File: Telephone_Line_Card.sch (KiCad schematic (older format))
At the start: 50 parts, among them J1 SULLINS EDGE 2X15 0.156\", J2 RJ11, K1 G5V-2, K2 TELTONE_M949-1, K3 G5V-2, Q6 2N3904, U1 4N35

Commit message: some schematic changes
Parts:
- removed C? (x2): 0.1uF, symbol Device:C
- removed C?: 0.047uF, symbol Device:C
- removed D?: 1N4148, Diode_THT:D_DO-35_SOD27_P7.62mm_Horizontal, symbol Diode:1N4148
- removed F?: Polyfuse, symbol Device:Polyfuse
- removed K1: G5V-2, Relay_THT:Relay_DPDT_Omron_G5V-2, symbol Relay:G5V-2
- removed Q?: 2N3904, Package_TO_SOT_THT:TO-92_Inline, symbol Transistor_BJT:2N3904
- removed R?: 10K, symbol Device:R_US
- removed R?: 1K, symbol Device:R_US
- removed TP1: GND, symbol Connector:TestPoint
- removed TP2: +12V, symbol Connector:TestPoint
- removed TP3: TESTPOINT(A), symbol Connector:TestPoint
- removed TP4: TESTPOINT(B), symbol Connector:TestPoint
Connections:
- net LINE1A is gone; now on net VOICE_LINE(T): J1.24 (Pin_24)
- net LINE1B is gone; now on net VOICE_LINE(R): J1.23 (Pin_23)
- net RING_TRIP: no longer J1.26 (Pin_26), R?.2, U1.5
- net VOICE_LINE(T): now reaches D?.1 (K), D?.2 (A)
- net VOICE_LINE(T): now also T?.8 (SB)
- net VOICE_LINE(R): now reaches D?.1 (K), D?.2 (A)
- net VOICE_LINE(R): now also T?.5 (SA)
- net LINE2A: no longer names the net of J1.22 (Pin_22)
- net LINE2B: no longer names the net of J1.21 (Pin_21)
- net LS: no longer names the net of J1.29 (Pin_29)
- net RING_BUS_R renamed RING_BUS(R)
- net RING_BUS_T renamed RING_BUS(T)
- new net RT: J1.26 (Pin_26), R?.2, U1.5
- no-connect marks 10 -> 13
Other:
- note added: "PROTOTYPE!"
- note removed: "*ADD RESISTORS INLINE?\n*ISOLATION TRANSFORMER \nBEFORE OR AFTER VOICE RELAY?"
- note removed: "PELIMINARY PROTOTYPE!"
- note removed: "VOICE LINE RELAY"
- moved on the sheet: D?

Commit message: some schematic changes
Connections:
- net RING_TRIP is gone; now on net RT: R?.1
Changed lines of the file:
@@
 Wire Wire Line
 	10320 3390 10610 3390
-Text Notes 11630 4290 0    50   ~ 0
+Text Notes 11640 4270 0    50   ~ 0
 RING TRIP CIRCUIT\nSEE "TRIX V2" FIG 19 FOR MORE DETAILS
 Text Notes 8390 8330 0    50   ~ 0
@@
 Wire Wire Line
 	10090 4960 10320 4960
-Text Notes 720  1500 0    500  ~ 0
+Text Notes 1410 1890 0    500  ~ 0
 PROTOTYPE!
 Connection ~ 11280 2740
@@
 	13390 7630 13390 8130
 Text GLabel 12570 8330 0    50   Input ~ 0
-RING_TRIP
+RT
 $Comp
 L Device:R_US R?

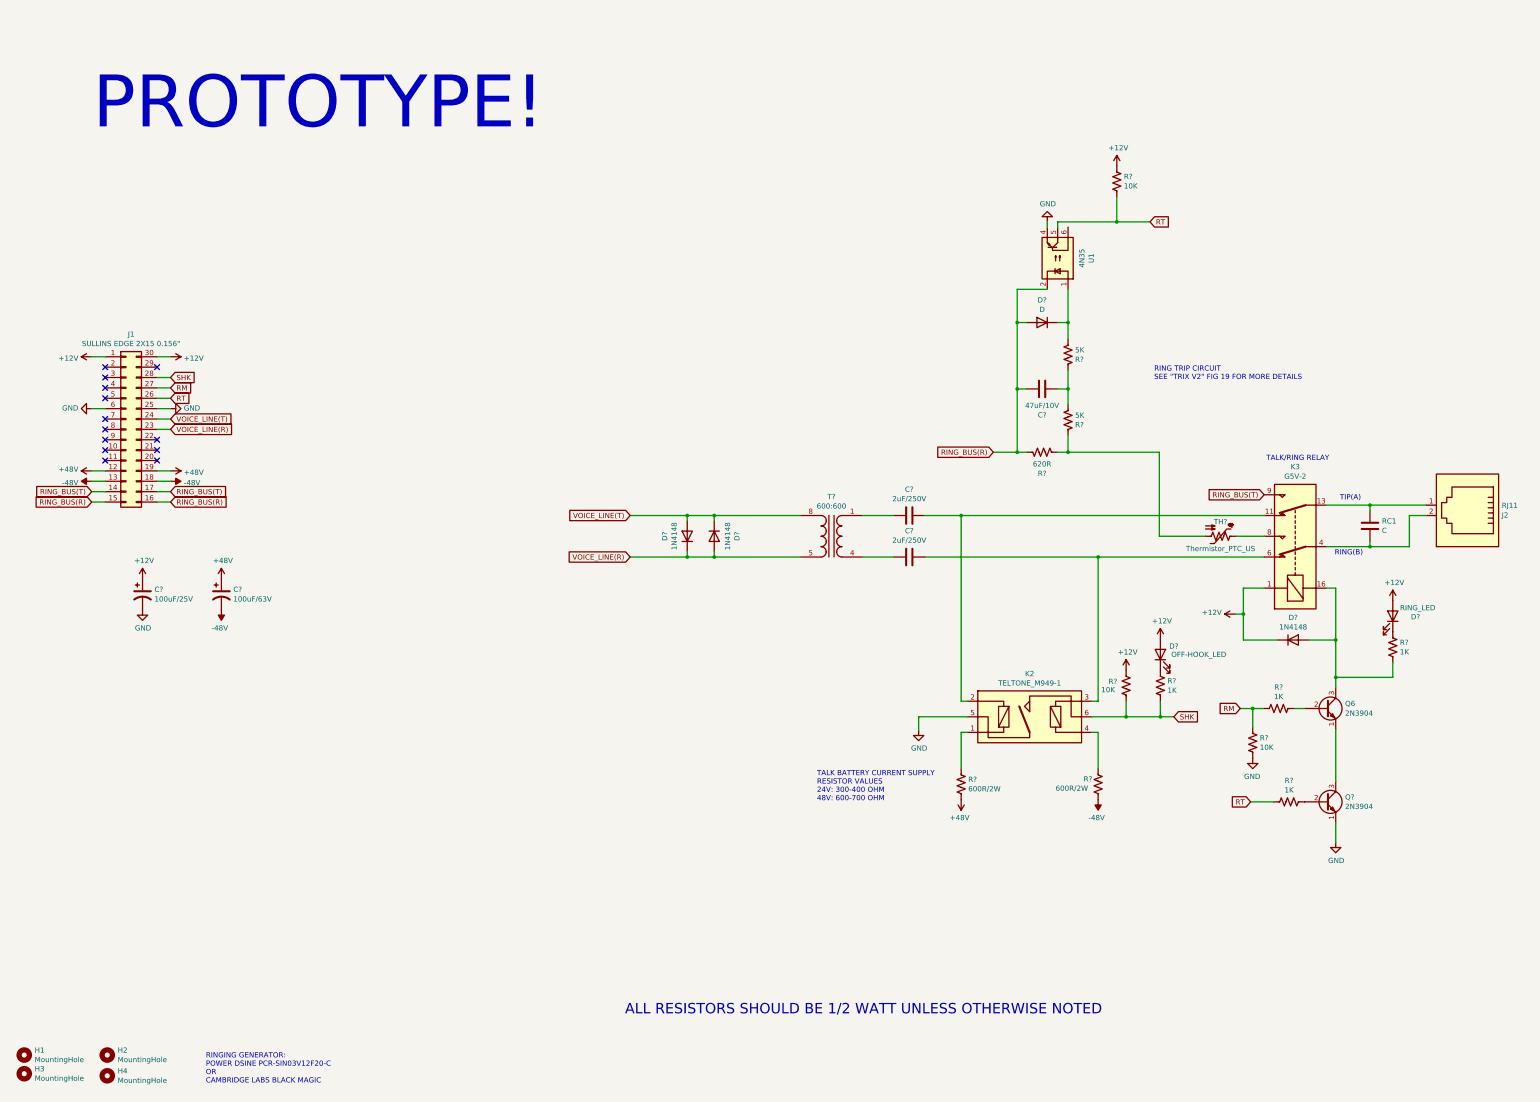
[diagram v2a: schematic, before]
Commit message: added slic sch symbol
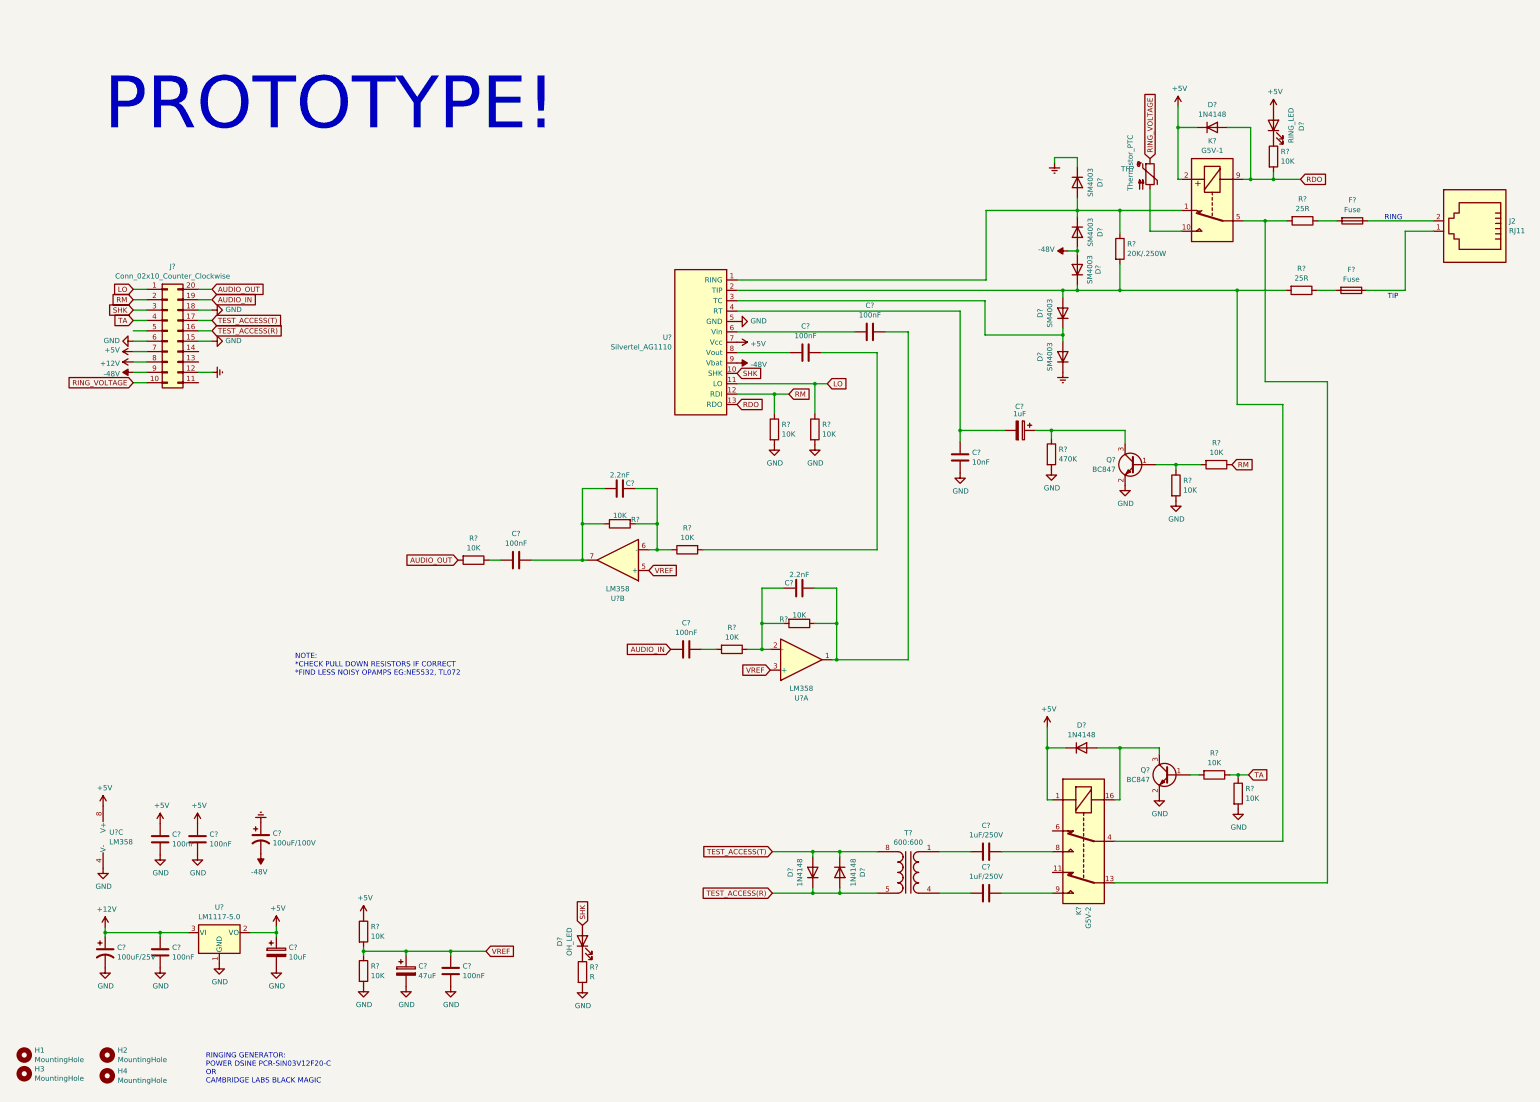
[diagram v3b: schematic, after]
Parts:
- removed C?: 47uF/10V, symbol Device:C
- removed D?: 1N4148, Diode_THT:D_DO-35_SOD27_P7.62mm_Horizontal, symbol Diode:1N4148
- removed D?: RING_LED, symbol Device:LED
- removed D?: D, symbol Device:D
- removed D?: OFF-HOOK_LED, symbol Device:LED
- removed J1: SULLINS EDGE 2X15 0.156\", symbol Connector_Generic:Conn_02x15_Counter_Clockwise
- removed K2: TELTONE_M949-1, symbol Relay_Line_Sense:TELTONE_M949-1
- removed K3: G5V-2, Relay_THT:Relay_DPDT_Omron_G5V-2, symbol Relay:G5V-2
- removed Q6, Q?: 2N3904, Package_TO_SOT_THT:TO-92_Inline, symbol Transistor_BJT:2N3904
- removed R? (x3): 10K, symbol Device:R_US
- removed R? (x4): 1K, symbol Device:R_US
- removed R?: 620R, symbol Device:R_US
- removed R? (x2): 5K, symbol Device:R_US
- removed R? (x2): 600R/2W, symbol Device:R_US
- removed RC1: C, symbol Device:C
- removed TH?: Thermistor_PTC_US, symbol Device:Thermistor_PTC_US
- removed U1: 4N35, Package_DIP:DIP-6_W7.62mm, symbol Isolator:4N35
- added C?: 1uF, symbol Device:CP
- added C?: 10nF, symbol Device:C
- added C? (x2): 2.2nF, symbol Device:C
- added C? (x8): 100nF, symbol Device:C
- added C?: 10uF, symbol Device:CP
- added C?: 47uF, symbol Device:CP
- added D? (x5): SM4003, Diode_SMD:D_MELF, symbol Diode:SM4003
- added D? (x2): 1N4148, Diode_THT:D_DO-35_SOD27_P7.62mm_Horizontal, symbol Diode:1N4148
- added D?: OH_LED, symbol Device:LED
- added D?: RING_LED, symbol Device:LED
- added F? (x2): Fuse, symbol Device:Fuse
- added J?: Conn_02x10_Counter_Clockwise, symbol Connector_Generic:Conn_02x10_Counter_Clockwise
- added K?: G5V-1, Relay_THT:Relay_SPDT_Omron_G5V-1, symbol Relay:G5V-1
- added K?: G5V-2, Relay_THT:Relay_DPDT_Omron_G5V-2, symbol Relay:G5V-2
- added Q? (x2): BC847, Package_TO_SOT_SMD:SOT-23, symbol Transistor_BJT:BC847
- added R? (x2): 25R, symbol Device:R
- added R?: 20K/.250W, symbol Device:R
- added R?: 470K, symbol Device:R
- added R? (x14): 10K, symbol Device:R
- added R?: R, symbol Device:R
- added TH?: Thermistor_PTC, symbol Device:Thermistor_PTC
- added U?: Silvertel_AG1110, symbol SLIC_Module:Silvertel_AG1110
- added U? (x3): LM358, symbol Amplifier_Operational:LM358
- added U?: LM1117-5.0, symbol Regulator_Linear:LM1117-5.0
- C? (x2): value 2uF/250V -> 1uF/250V
- C?: value 100uF/63V -> 100uF/100V
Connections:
- net +12V: now also C?.1, J?.8 (Pin_8), U?.3 (VI)
- net -48V: now also D?.2 (A), D?.2 (A), J?.9 (Pin_9), U?.9 (Vbat)
- net GND: now also C?.2, C?.2, C?.2, C?.2, C?.2, C?.2, C?.2, J?.15 (Pin_15), J?.18 (Pin_18), J?.6 (Pin_6), Q?.2 (E), Q?.2 (E), R?.2, R?.2, R?.2, R?.2, R?.2, R?.2, R?.2, U?.1 (GND), U?.4 (V-), U?.5 (GND)
- net RM: now also J?.2 (Pin_2), R?.1, R?.1, U?.12 (RDI)
- net SHK: now also D?.2 (A), J?.3 (Pin_3), U?.10 (SHK)
- net at J2.1: now also F?.1
- net at J2.2: now also F?.1
- net at C?.1: now also K?.8
- net at C?.1: now also K?.9
- net +48V renamed Earth
- net Earth: now also D?.1 (K), D?.1 (K), J?.12 (Pin_12)
- net VOICE_LINE(R) renamed TEST_ACCESS(R)
- net TEST_ACCESS(R): now also J?.16 (Pin_16)
- net VOICE_LINE(T) renamed TEST_ACCESS(T)
- net TEST_ACCESS(T): now also J?.17 (Pin_17)
- new net: D?.1 (K), D?.2 (A), K?.1, R?.1, U?.1 (RING)
- new net: D?.1 (K), D?.2 (A), K?.4, R?.2, R?.2, U?.2 (TIP)
- new net: D?.1 (K), D?.2 (A), U?.3 (TC)
- new net: C?.1, C?.2, U?.4 (RT)
- new net: C?.2, U?.6 (Vin)
- new net: C?.1, U?.8 (Vout)
- new net: F?.2, R?.1 (x2)
- new net: K?.13, K?.5, K?.6, R?.2
- new net: K?.10, TH?.2
- new net: C?.1, Q?.3 (C), R?.1
- new net: Q?.1 (B), R?.1, R?.2
- new net: D?.2 (A), K?.16, Q?.3 (C)
- new net: Q?.1 (B), R?.2
- new net: C?.1, C?.1, R?.1, U?.1
- new net: C?.2, R?.1, R?.2, U?.2 (-)
- new net: C?.2, R?.1, R?.2, U?.6 (-)
- new net: C?.1, C?.1, R?.1, U?.7
- new net: C?.2, R?.2
- new net: C?.2, R?.1
- new net: C?.1, R?.2
- new net: D?.1 (K), R?.1 (x2)
- new net +5V: C?.1, C?.1, C?.1, D?.1 (K), D?.1 (K), D?.2 (A), J?.7 (Pin_7), K?.1, K?.2, R?.1, U?.2 (VO), U?.7 (Vcc), U?.8 (V+)
- new net AUDIO_IN: C?.2, J?.19 (Pin_19)
- new net AUDIO_OUT: J?.20 (Pin_20), R?.2
- new net LO: J?.1 (Pin_1), R?.1, U?.11 (LO)
- new net RDO: D?.2 (A), K?.9, R?.2, U?.13 (RDO)
- new net RING_VOLTAGE: J?.10 (Pin_10), TH?.1
- new net TA: J?.4 (Pin_4), R?.1, R?.1
- new net VREF: C?.1, C?.1, R?.1, R?.2, U?.3 (+), U?.5 (+)
- no-connect marks 13 -> 0
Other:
- note added: "NOTE:\n*CHECK PULL DOWN RESISTORS IF CORRECT\n*FIND LESS NOISY OPAMPS EG:NE5532, TL072"
- note added: "RING"
- note added: "TIP"
- note removed: "ALL RESISTORS SHOULD BE 1/2 WATT UNLESS OTHERWISE NOTED"
- note removed: "RING TRIP CIRCUIT\nSEE "TRIX V2" FIG 19 FOR MORE DETAILS"
- note removed: "RING(B)"
- note removed: "TALK BATTERY CURRENT SUPPLY\nRESISTOR VALUES\n24V: 300-400 OHM\n48V: 600-700 OHM"
- note removed: "TALK/RING RELAY"
- note removed: "TIP(A)"
- moved on the sheet: C?, D?, J2, T?

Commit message: some changes
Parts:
- removed C? (x2): 1uF/250V, symbol Device:C
- removed C?: 100uF/100V, symbol Device:CP1
- removed C?: 100uF/25V, symbol Device:CP1
- removed C?: 1uF, symbol Device:CP
- removed C?: 10nF, symbol Device:C
- removed C? (x2): 2.2nF, symbol Device:C
- removed C? (x8): 100nF, symbol Device:C
- removed C?: 10uF, symbol Device:CP
- removed C?: 47uF, symbol Device:CP
- removed D? (x5): SM4003, Diode_SMD:D_MELF, symbol Diode:SM4003
- removed D? (x4): 1N4148, Diode_THT:D_DO-35_SOD27_P7.62mm_Horizontal, symbol Diode:1N4148
- removed D?: OH_LED, symbol Device:LED
- removed D?: RING_LED, symbol Device:LED
- removed F? (x2): Fuse, symbol Device:Fuse
- removed J?: Conn_02x10_Counter_Clockwise, symbol Connector_Generic:Conn_02x10_Counter_Clockwise
- removed K?: G5V-1, Relay_THT:Relay_SPDT_Omron_G5V-1, symbol Relay:G5V-1
- removed K?: G5V-2, Relay_THT:Relay_DPDT_Omron_G5V-2, symbol Relay:G5V-2
- removed Q? (x2): BC847, Package_TO_SOT_SMD:SOT-23, symbol Transistor_BJT:BC847
- removed R? (x2): 25R, symbol Device:R
- removed R?: 20K/.250W, symbol Device:R
- removed R?: 470K, symbol Device:R
- removed R? (x14): 10K, symbol Device:R
- removed R?: R, symbol Device:R
- removed T?: 600:600, symbol Device:Transformer_1P_1S_SO8
- removed TH?: Thermistor_PTC, symbol Device:Thermistor_PTC
- removed U?: Silvertel_AG1110, symbol SLIC_Module:Silvertel_AG1110
- removed U? (x3): LM358, symbol Amplifier_Operational:LM358
- removed U?: LM1117-5.0, symbol Regulator_Linear:LM1117-5.0
- added C1: 100uF, Capacitor_THT:CP_Radial_D8.0mm_P5.00mm, symbol Device:CP1
- added C2: 100uF/100V, Capacitor_THT:CP_Radial_D12.5mm_P5.00mm, symbol Device:CP1
- added C3: 0.1uF, Capacitor_THT:C_Disc_D4.7mm_W2.5mm_P5.00mm, symbol Device:C
- added C4, C5: 2uF/100V, Capacitor_THT:C_Rect_L18.0mm_W8.0mm_P15.00mm_FKS3_FKP3, symbol Device:C
- added C6: RC .1uF/47R, Capacitor_THT:C_Rect_L24.0mm_W10.9mm_P22.50mm_MKT, symbol Device:C
- added C7: 47uF/10V, Capacitor_THT:C_Radial_D10.0mm_H12.5mm_P5.00mm, symbol Device:C
- added D1: OFFHOOK_LED, LED_THT:LED_D5.0mm, symbol Device:LED
- added D2: RING_LED, LED_THT:LED_D5.0mm, symbol Device:LED
- added D3, D4, D5, D6: 1N4148, Diode_THT:D_DO-35_SOD27_P7.62mm_Horizontal, symbol Diode:1N4148
- added J1: Conn_01x12, Connector_PinSocket_2.54mm:PinSocket_1x12_P2.54mm_Vertical, symbol Connector_Generic:Conn_01x12
- added K1: TELTONE_M949-1, Teltone_M949_Line_Sense_Relay:Teltone_M-949-1, symbol Relay_Line_Sense:TELTONE_M949-1
- added K2: G5V-2, Relay_THT:Relay_DPDT_Omron_G5V-2, symbol Relay:G5V-2
- added Q1: 2N3904, Package_TO_SOT_THT:TO-92_Wide, symbol Transistor_BJT:2N3904
- added R1, R2: 330R/2W, Resistor_THT:R_Axial_DIN0617_L17.0mm_D6.0mm_P30.48mm_Horizontal, symbol Device:R_US
- added R10, R9: 5K, Resistor_THT:R_Axial_DIN0309_L9.0mm_D3.2mm_P12.70mm_Horizontal, symbol Device:R_US
- added R11, R6, R7: 10K, Resistor_THT:R_Axial_DIN0309_L9.0mm_D3.2mm_P12.70mm_Horizontal, symbol Device:R_US
- added R3, R4, R5: 1K, Resistor_THT:R_Axial_DIN0309_L9.0mm_D3.2mm_P12.70mm_Horizontal, symbol Device:R_US
- added R8: 620R, Resistor_THT:R_Axial_DIN0309_L9.0mm_D3.2mm_P12.70mm_Horizontal, symbol Device:R_US
- added T1: 600:600, Transformer_Bourns_LM-NP-100x_Signal_Transformers:Transformer_Bourns_LM-NP-1001_1xSec, symbol Device:Transformer_1P_1S_SO8
- added TH1: Thermistor_PTC, Fuse:Fuse_Bourns_MF-RG400, symbol Device:Thermistor_PTC_US
- added U1: 4N35, Package_DIP:DIP-6_W7.62mm, symbol Isolator:4N35
- H1, H2, H3, H4: footprint (none) -> MountingHole:MountingHole_3.2mm_M3
- J2: footprint (none) -> TerminalBlock:TerminalBlock_bornier-2_P5.08mm
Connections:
- net +5V: now also C1.1, D1.2 (A), D2.2 (A), D3.1 (K), J1.6 (Pin_6), K2.1, R11.1, R7.1
- net Earth: now also C2.1, J1.9 (Pin_9), R1.2
- net GND: now also C1.2, J1.7 (Pin_7), K1.5, Q1.1 (E), R6.2, U1.4
- net RM: now also J1.3 (Pin_3), R5.2, R6.1
- net SHK: now also J1.4 (Pin_4), K1.6, R3.2, R7.2
- net at J2.1: now also C6.1, K2.13
- net at J2.2: now also C6.2, K2.4
- new net: C4.1, K1.2, K2.11
- new net: D3.2 (A), K2.16, Q1.3 (C), R4.2
- new net: C5.1, K1.3, K2.6
- new net: K2.8, TH1.1
- new net: D2.1 (K), R4.1
- new net: Q1.2 (B), R5.1
- new net: R8.1, R9.2, TH1.2
- new net: C7.1, R10.2, R9.1
- new net: D6.1 (K), R10.1, U1.1
- new net: K1.1, R1.1
- new net: K1.4, R2.1
- new net: C4.2, T1.1 (AA)
- new net: C5.2, T1.4 (AB)
- new net: C3.1, D4.1 (K), D5.2 (A), T1.8 (SB)
- new net: D1.1 (K), R3.1
- new net -24V: C2.2, J1.8 (Pin_8), R2.2
- new net RING_BUS(R): C7.2, D6.2 (A), J1.12 (Pin_12), R8.2, U1.2
- new net RING_BUS(T): J1.11 (Pin_11), K2.9
- new net RT: J1.5 (Pin_5), R11.2, U1.5
- new net VOICE_LINE(R): D4.2 (A), D5.1 (K), J1.2 (Pin_2), T1.5 (SA)
- new net VOICE_LINE(T): C3.2, J1.1 (Pin_1)
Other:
- note added: "RING(B)"
- note added: "TALK BATTERY CURRENT SUPPLY\nR1-R2 RESISTOR VALUES\n24V: 300-400 OHM\n48V: 600-700 OHM"
- note added: "TIP(A)"
- note removed: "NOTE:\n*CHECK PULL DOWN RESISTORS IF CORRECT\n*FIND LESS NOISY OPAMPS EG:NE5532, TL072"
- note removed: "PROTOTYPE!"
- note removed: "RING"
- note removed: "TIP"

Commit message: some pcb changes
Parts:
- J1: footprint Connector_PinSocket_2.54mm:PinSocket_1x12_P2.54mm_Vertical -> Connector_PinSocket_2.54mm:PinSocket_1x12_P2.54mm_Horizontal
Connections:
- net -24V: now also J1.9 (Pin_9); no longer J1.8 (Pin_8)
- net Earth: now also J1.10 (Pin_10); no longer J1.9 (Pin_9)
- net GND: now also J1.8 (Pin_8)
- net RING_BUS(T): now also K2.8; no longer K2.9
- net RT: now also J1.2 (Pin_2); no longer J1.5 (Pin_5)
- net SHK: now also J1.1 (Pin_1); no longer J1.4 (Pin_4)
- net VOICE_LINE(R): now also J1.5 (Pin_5), T1.8 (SB); no longer J1.2 (Pin_2), T1.5 (SA)
- net VOICE_LINE(T): now also J1.4 (Pin_4); no longer J1.1 (Pin_1)
- net at C6.1, J2.1: now also K2.4; no longer K2.13
- net at C6.2, J2.2: now also K2.13; no longer K2.4
- net at C4.1, K1.2: now also K2.6; no longer K2.11
- net at C5.1, K1.3: now also K2.11; no longer K2.6
- net at TH1.1: now also K2.9; no longer K2.8
- net at T1.1 (AA): now also C5.2; no longer C4.2
- net at T1.4 (AB): now also C4.2; no longer C5.2
- net at C3.1, D4.1 (K), D5.2 (A): now also T1.5 (SA); no longer T1.8 (SB)
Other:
- moved on the sheet: C6, D2, D3, J2, K2, Q1, R4, R5, R6, TH1
